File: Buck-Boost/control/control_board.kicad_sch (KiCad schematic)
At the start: 65 parts, among them IC1 F2800137RGZR, J1 Conn_01x05_Header, J8 Conn_01x02_Pin, J9 Conn_02x04_Counter_Clockwise, U1 LMV321, U10 LMV321, U2 TPS562202, U6 IR2101, U7 TCAN3414DR, U8 LD1117S12TR_SOT223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

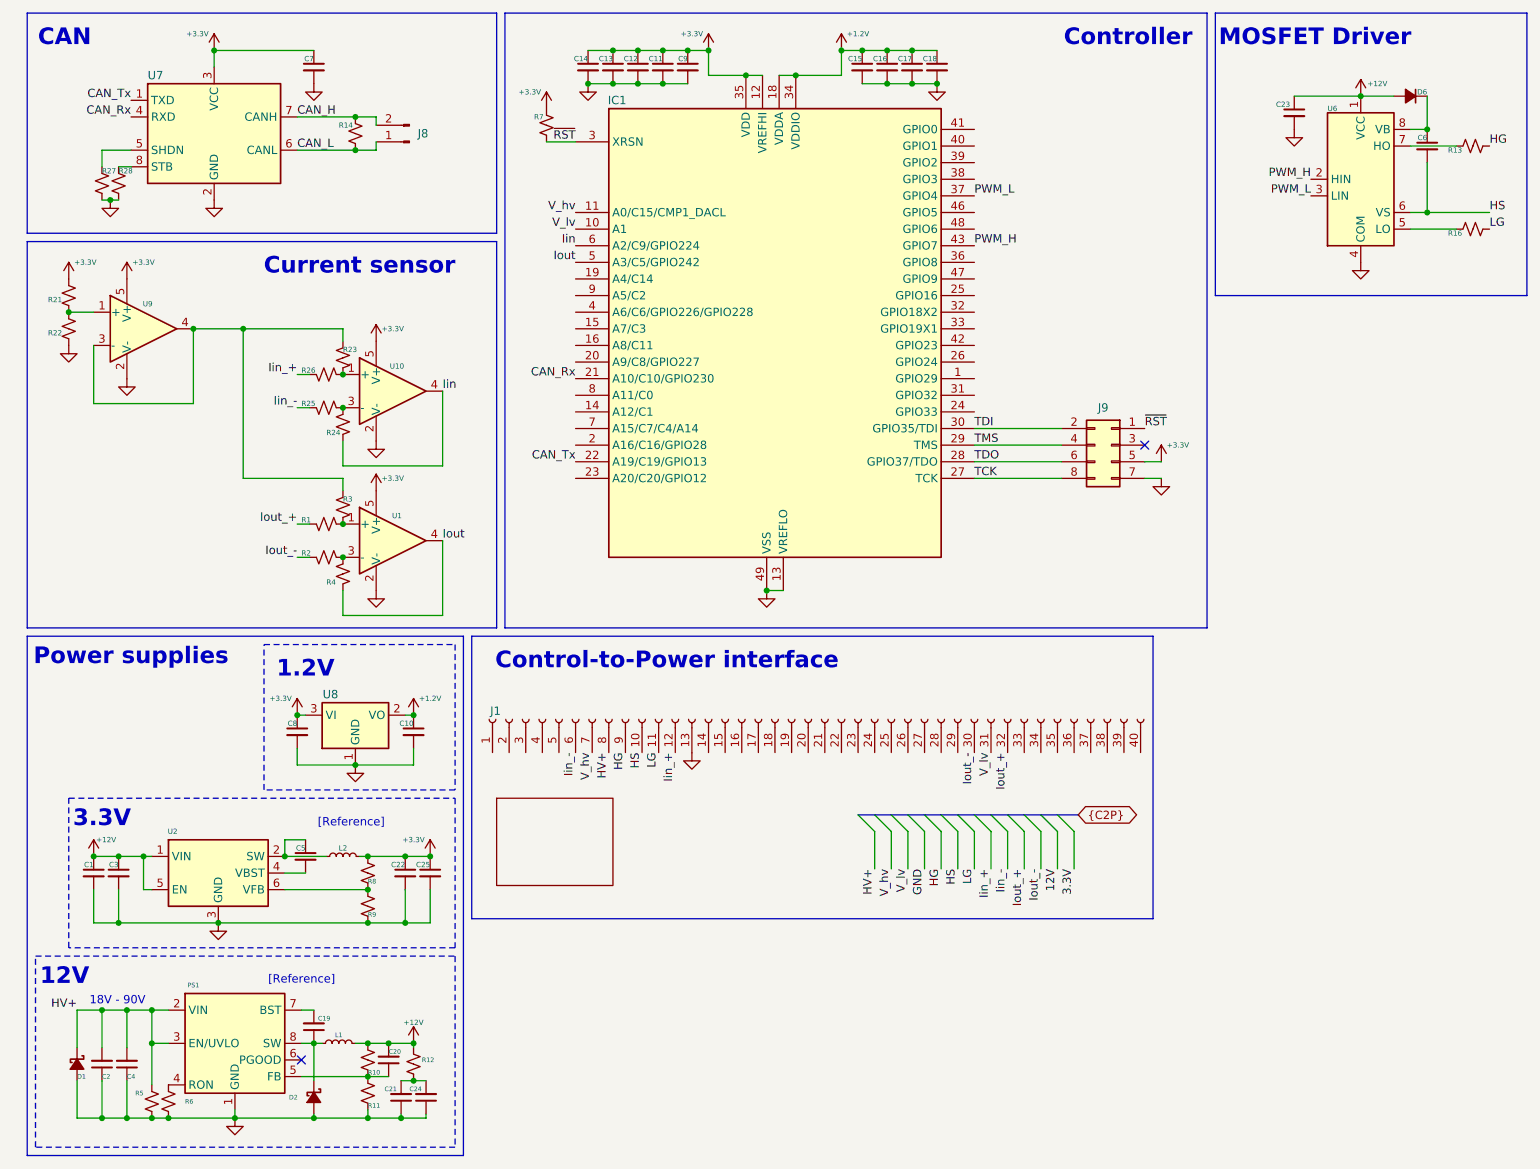
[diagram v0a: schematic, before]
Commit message: buck-boost/control & buck-boost/variant1 - corrected the pin-config
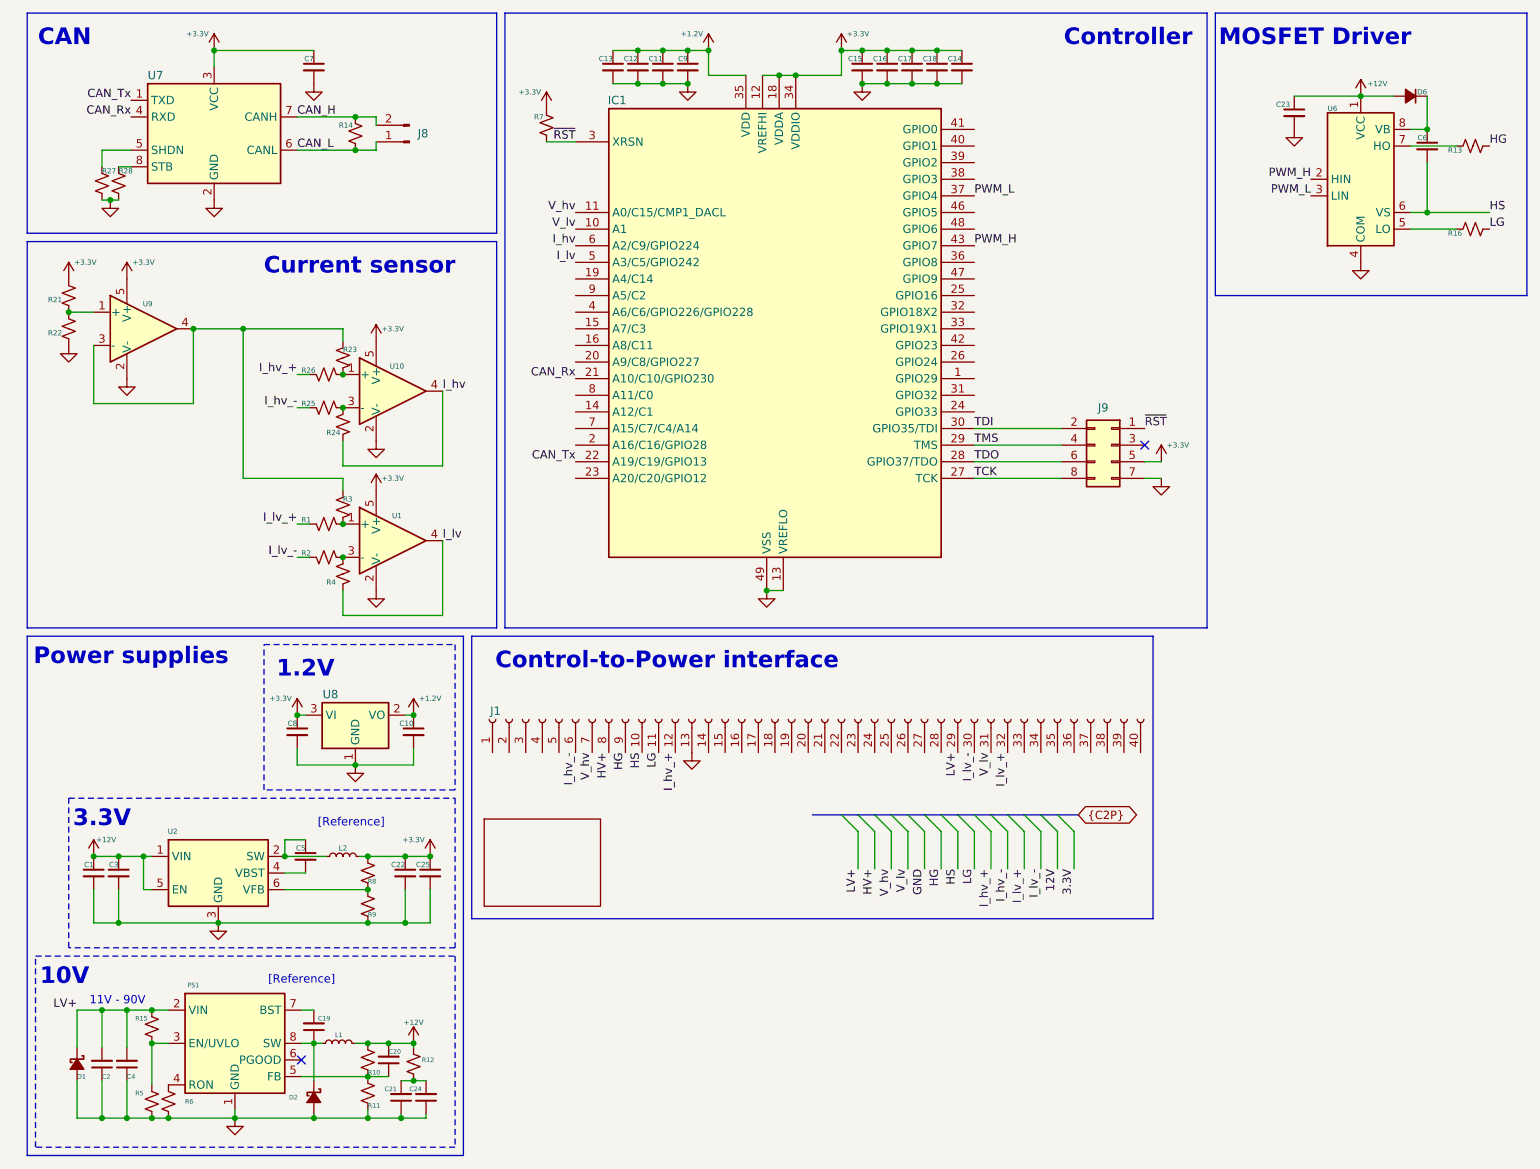
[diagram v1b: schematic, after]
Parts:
- added R15: 100K, >=62.5mW, 0402, Resistor_SMD:R_0805_2012Metric, symbol Device:R_Small_US
- R10: value 453K, >=62.5mW, 0402 -> 732K, >=62.5mW, 0402; MPN mcmr04x4533ftl -> (none); Vendor https://in.element14.com/multicomp-pro/mcmr04x4533ftl/res-4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 -> (none)
- R11: value 49.9K, >=62.5mW, 0402 -> 101K, >=62.5mW, 0402; MPN mcwr04x4992ftl -> (none); Vendor https://in.element14.com/multicomp-pro/mcwr04x4992ftl/res-4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 -> (none)
- R5: value 10K, >=62.5mW, 0402 -> 16.9K, >=62.5mW, 0402; MPN mcwr04x1002ftl -> (none); Vendor https://in.element14.com/multicomp/mcwr04x1002ftl/res-10k-1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 -> (none)
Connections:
- net +1.2V: now also C11.1, C12.1, C13.1, C9.1, IC1.35 (VDD), IC1.44 (VDD); no longer C15.1, C16.1, C17.1, C18.1, IC1.18 (VDDA), IC1.34 (VDDIO), IC1.45 (VDDIO)
- net +3.3V: now also C15.1, C16.1, C17.1, C18.1, IC1.18 (VDDA), IC1.34 (VDDIO), IC1.45 (VDDIO); no longer C11.1, C12.1, C13.1, C9.1, IC1.35 (VDD), IC1.44 (VDD)
- net HV+: no longer C2.2, C4.2, D1.1 (K), PS1.2 (VIN), PS1.3 (EN/UVLO), R5.1
- net LV+: now reaches J1.29 (Pin_29)
- net LV+: now also C2.2, C4.2, D1.1 (K), PS1.2 (VIN), R15.1
- net Iin renamed I_hv
- net Iin_+ renamed I_hv_+
- net Iin_- renamed I_hv_-
- net Iout renamed I_lv
- net Iout_+ renamed I_lv_+
- net Iout_- renamed I_lv_-
- new net: PS1.3 (EN/UVLO), R15.2, R5.1
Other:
- note added: "10V"
- note added: "11V - 90V"
- note removed: "12V"
- note removed: "18V - 90V"
